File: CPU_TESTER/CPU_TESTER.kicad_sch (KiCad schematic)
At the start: 27 parts, among them J1 Conn_02x21_Odd_Even, J2 Conn_02x21_Odd_Even, J3 Conn_02x21_Odd_Even, J4 Conn_02x21_Odd_Even, J5 Conn_02x21_Odd_Even, J6 Conn_02x21_Odd_Even, J7 Conn_02x21_Odd_Even, Q1 2N3904, Q2 2N3904, Q3 2N3904

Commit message: CPU tester design
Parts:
- R2, R3, R4, R5, R6, R7: value 10.1K -> 10.5K
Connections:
- net 12V_MON: now also A1.26 (A7); no longer A1.19 (A0)
- net BD_EN0: now also A1.24 (A5); no longer A1.5 (D2)
- net BD_EN1: now also A1.23 (A4); no longer A1.6 (D3)
- net BD_EN2: now also A1.22 (A3); no longer A1.7 (D4)
- net BD_EN3: now also A1.21 (A2); no longer A1.8 (D5)
- net BD_EN4: now also A1.20 (A1); no longer A1.9 (D6)
- net BD_EN5: now also A1.19 (A0); no longer A1.10 (D7)
- net BD_ENM: now also A1.15 (D12); no longer A1.11 (D8)
- net IRQ_0: now also A1.10 (D7); no longer A1.12 (D9)
- net IRQ_1: now also A1.11 (D8); no longer A1.13 (D10)
- net LED_0: now also A1.6 (D3); no longer A1.20 (A1)
- net LED_1: now also A1.8 (D5); no longer A1.21 (A2)
- net LED_2: now also A1.9 (D6); no longer A1.22 (A3)
- net LED_3: now also A1.12 (D9); no longer A1.23 (A4)
- net LED_4: now also A1.13 (D10); no longer A1.24 (A5)
- net LED_5: now also A1.14 (D11); no longer A1.25 (A6)
- net LED_C: now also A1.5 (D2); no longer A1.26 (A7)
- net RST: now also A1.7 (D4); no longer A1.14 (D11)
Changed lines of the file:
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@@
   (no_connect (at 86.36 112.395))
   (no_connect (at 91.44 112.395))
-  (no_connect (at 76.2 153.035))
+  (no_connect (at 101.6 153.035))
   (no_connect (at 76.2 122.555))
   (no_connect (at 76.2 125.095))
@@
     (stroke (width 0) (type default) (color 0 0 0 0))
   )
-  (wire (pts (xy 101.6 153.035) (xy 109.855 153.035))
+  (wire (pts (xy 67.31 153.035) (xy 76.2 153.035))
     (stroke (width 0) (type default) (color 0 0 0 0))
   )
@@
     (effects (font (size 1.27 1.27)) (justify right bottom))
   )
-  (label "BD_EN1" (at 67.31 130.175 0)
-    (effects (font (size 1.27 1.27)) (justify left bottom))
+  (label "BD_EN1" (at 109.855 147.955 180)
+    (effects (font (size 1.27 1.27)) (justify right bottom))
   )
   (label "12V_MON" (at 61.595 93.345 180)
     (effects (font (size 1.27 1.27)) (justify right bottom))
   )
-  (label "IRQ_1" (at 67.31 147.955 0)
+  (label "IRQ_1" (at 67.31 142.875 0)
     (effects (font (size 1.27 1.27)) (justify left bottom))
   )
-  (label "12V_MON" (at 109.855 137.795 180)
+  (label "12V_MON" (at 109.855 155.575 180)
     (effects (font (size 1.27 1.27)) (justify right bottom))
   )
@@
     (effects (font (size 1.27 1.27)) (justify right bottom))
   )
-  (label "BD_EN3" (at 67.31 135.255 0)
-    (effects (font (size 1.27 1.27)) (justify left bottom))
+  (label "BD_EN3" (at 109.855 142.875 180)
+    (effects (font (size 1.27 1.27)) (justify right bottom))
   )
-  (label "BD_ENM" (at 67.31 142.875 0)
+  (label "BD_ENM" (at 67.31 153.035 0)
     (effects (font (size 1.27 1.27)) (justify left bottom))
   )
@@
     (effects (font (size 1.27 1.27)) (justify right bottom))
   )
-  (label "BD_EN5" (at 67.31 140.335 0)
-    (effects (font (size 1.27 1.27)) (justify left bottom))
-  )
-  (label "LED_C" (at 109.855 155.575 180)
+  (label "BD_EN5" (at 109.855 137.795 180)
     (effects (font (size 1.27 1.27)) (justify right bottom))
   )
+  (label "LED_C" (at 67.31 127.635 0)
+    (effects (font (size 1.27 1.27)) (justify left bottom))
+  )
   (label "IRQ_1" (at 127.635 135.89 0)
     (effects (font (size 1.27 1.27)) (justify left bottom))
   )
-  (label "LED_1" (at 109.855 142.875 180)
-    (effects (font (size 1.27 1.27)) (justify right bottom))
+  (label "LED_1" (at 67.31 135.255 0)
+    (effects (font (size 1.27 1.27)) (justify left bottom))
   )
   (label "IRQ_0" (at 110.49 110.49 0)
     (effects (font (size 1.27 1.27)) (justify left bottom))
   )
-  (label "LED_3" (at 109.855 147.955 180)
-    (effects (font (size 1.27 1.27)) (justify right bottom))
+  (label "LED_3" (at 67.31 145.415 0)
+    (effects (font (size 1.27 1.27)) (justify left bottom))
   )
-  (label "RST" (at 67.31 150.495 0)
+  (label "RST" (at 67.31 132.715 0)
     (effects (font (size 1.27 1.27)) (justify left bottom))
   )
@@
     (effects (font (size 1.27 1.27)) (justify right bottom))
   )
-  (label "LED_4" (at 109.855 150.495 180)
-    (effects (font (size 1.27 1.27)) (justify right bottom))
-  )
-  (label "IRQ_0" (at 67.31 145.415 0)
+  (label "LED_4" (at 67.31 147.955 0)
     (effects (font (size 1.27 1.27)) (justify left bottom))
   )
-  (label "BD_EN2" (at 67.31 132.715 0)
+  (label "IRQ_0" (at 67.31 140.335 0)
     (effects (font (size 1.27 1.27)) (justify left bottom))
   )
-  (label "LED_0" (at 109.855 140.335 180)
+  (label "BD_EN2" (at 109.855 145.415 180)
     (effects (font (size 1.27 1.27)) (justify right bottom))
   )
+  (label "LED_0" (at 67.31 130.175 0)
+    (effects (font (size 1.27 1.27)) (justify left bottom))
+  )
   (label "LED_3" (at 44.45 150.495 180)
     (effects (font (size 1.27 1.27)) (justify right bottom))
   )
-  (label "BD_EN0" (at 67.31 127.635 0)
-    (effects (font (size 1.27 1.27)) (justify left bottom))
-  )
-  (label "BD_EN4" (at 67.31 137.795 0)
-    (effects (font (size 1.27 1.27)) (justify left bottom))
+  (label "BD_EN0" (at 109.855 150.495 180)
+    (effects (font (size 1.27 1.27)) (justify right bottom))
   )
-  (label "LED_2" (at 109.855 145.415 180)
+  (label "BD_EN4" (at 109.855 140.335 180)
     (effects (font (size 1.27 1.27)) (justify right bottom))
   )
+  (label "LED_2" (at 67.31 137.795 0)
+    (effects (font (size 1.27 1.27)) (justify left bottom))
+  )
   (label "LED_0" (at 44.45 110.49 180)
     (effects (font (size 1.27 1.27)) (justify right bottom))
   )
-  (label "LED_5" (at 109.855 153.035 180)
-    (effects (font (size 1.27 1.27)) (justify right bottom))
+  (label "LED_5" (at 67.31 150.495 0)
+    (effects (font (size 1.27 1.27)) (justify left bottom))
   )
   (label "LED_2" (at 44.45 137.16 180)
@@
     (in_bom yes) (on_board yes) (fields_autoplaced)
     (property "Reference" "R2" (id 0) (at 121.285 104.14 90))
-    (property "Value" "10.1K" (id 1) (at 121.285 106.68 90))
+    (property "Value" "10.5K" (id 1) (at 121.285 106.68 90))
     (property "Footprint" "Resistor_THT:R_Axial_DIN0207_L6.3mm_D2.5mm_P10.16mm_Horizontal" (id 2) (at 121.285 112.268 90)
       (effects (font (size 1.27 1.27)) hide)
@@
       (effects (font (size 1.27 1.27)) (justify left))
     )
-    (property "Value" "10.1K" (id 1) (at 154.305 165.7349 0)
+    (property "Value" "10.5K" (id 1) (at 154.305 165.7349 0)
       (effects (font (size 1.27 1.27)) (justify left))
     )
@@
       (effects (font (size 1.27 1.27)) (justify left))
     )
-    (property "Value" "10.1K" (id 1) (at 154.305 125.7299 0)
+    (property "Value" "10.5K" (id 1) (at 154.305 125.7299 0)
       (effects (font (size 1.27 1.27)) (justify left))
     )
@@
     (in_bom yes) (on_board yes) (fields_autoplaced)
     (property "Reference" "R5" (id 0) (at 139.065 169.545 90))
-    (property "Value" "10.1K" (id 1) (at 139.065 172.085 90))
+    (property "Value" "10.5K" (id 1) (at 139.065 172.085 90))
     (property "Footprint" "Resistor_THT:R_Axial_DIN0207_L6.3mm_D2.5mm_P10.16mm_Horizontal" (id 2) (at 139.065 177.673 90)
       (effects (font (size 1.27 1.27)) hide)
@@
       (effects (font (size 1.27 1.27)) (justify left))
     )
-    (property "Value" "10.1K" (id 1) (at 136.525 100.3299 0)
+    (property "Value" "10.5K" (id 1) (at 136.525 100.3299 0)
       (effects (font (size 1.27 1.27)) (justify left))
     )
@@
     (in_bom yes) (on_board yes) (fields_autoplaced)
     (property "Reference" "R4" (id 0) (at 139.065 129.54 90))
-    (property "Value" "10.1K" (id 1) (at 139.065 132.08 90))
+    (property "Value" "10.5K" (id 1) (at 139.065 132.08 90))
     (property "Footprint" "Resistor_THT:R_Axial_DIN0207_L6.3mm_D2.5mm_P10.16mm_Horizontal" (id 2) (at 139.065 137.668 90)
       (effects (font (size 1.27 1.27)) hide)
@@
     )
     (path "/146bb74a-c5dc-4101-86b1-cd35181b91ef"
-      (reference "R2") (unit 1) (value "10.1K") (footprint "Resistor_THT:R_Axial_DIN0207_L6.3mm_D2.5mm_P10.16mm_Horizontal")
+      (reference "R2") (unit 1) (value "10.5K") (footprint "Resistor_THT:R_Axial_DIN0207_L6.3mm_D2.5mm_P10.16mm_Horizontal")
     )
     (path "/dd175bfa-b3ad-4339-abd5-bbb7c0154b85"
-      (reference "R3") (unit 1) (value "10.1K") (footprint "Resistor_THT:R_Axial_DIN0207_L6.3mm_D2.5mm_P10.16mm_Horizontal")
+      (reference "R3") (unit 1) (value "10.5K") (footprint "Resistor_THT:R_Axial_DIN0207_L6.3mm_D2.5mm_P10.16mm_Horizontal")
     )
     (path "/ede24277-117d-4b1a-99a2-30baade9bd49"
-      (reference "R4") (unit 1) (value "10.1K") (footprint "Resistor_THT:R_Axial_DIN0207_L6.3mm_D2.5mm_P10.16mm_Horizontal")
+      (reference "R4") (unit 1) (value "10.5K") (footprint "Resistor_THT:R_Axial_DIN0207_L6.3mm_D2.5mm_P10.16mm_Horizontal")
     )
     (path "/c0a6a793-23e6-4787-a4b7-0b60fe74897d"
-      (reference "R5") (unit 1) (value "10.1K") (footprint "Resistor_THT:R_Axial_DIN0207_L6.3mm_D2.5mm_P10.16mm_Horizontal")
+      (reference "R5") (unit 1) (value "10.5K") (footprint "Resistor_THT:R_Axial_DIN0207_L6.3mm_D2.5mm_P10.16mm_Horizontal")
     )
     (path "/ac35a4cd-ee98-4a72-92c9-79826d438297"
-      (reference "R6") (unit 1) (value "10.1K") (footprint "Resistor_THT:R_Axial_DIN0207_L6.3mm_D2.5mm_P10.16mm_Horizontal")
+      (reference "R6") (unit 1) (value "10.5K") (footprint "Resistor_THT:R_Axial_DIN0207_L6.3mm_D2.5mm_P10.16mm_Horizontal")
     )
     (path "/9bdb9f7f-025a-4cbb-add4-7af250ed0474"
-      (reference "R7") (unit 1) (value "10.1K") (footprint "Resistor_THT:R_Axial_DIN0207_L6.3mm_D2.5mm_P10.16mm_Horizontal")
+      (reference "R7") (unit 1) (value "10.5K") (footprint "Resistor_THT:R_Axial_DIN0207_L6.3mm_D2.5mm_P10.16mm_Horizontal")
     )
     (path "/27ba8598-88b0-4157-a7a7-e1e74e09d01a"

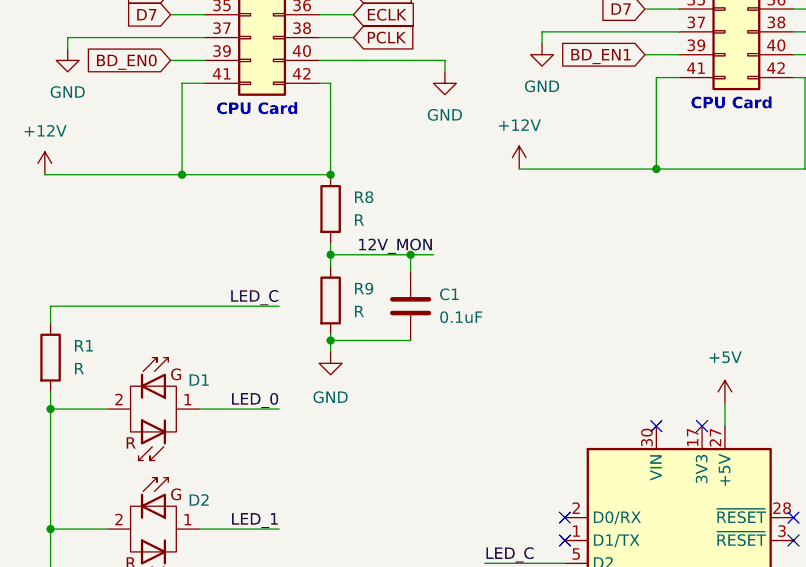
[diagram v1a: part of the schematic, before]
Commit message: Updated tester schematic, per built
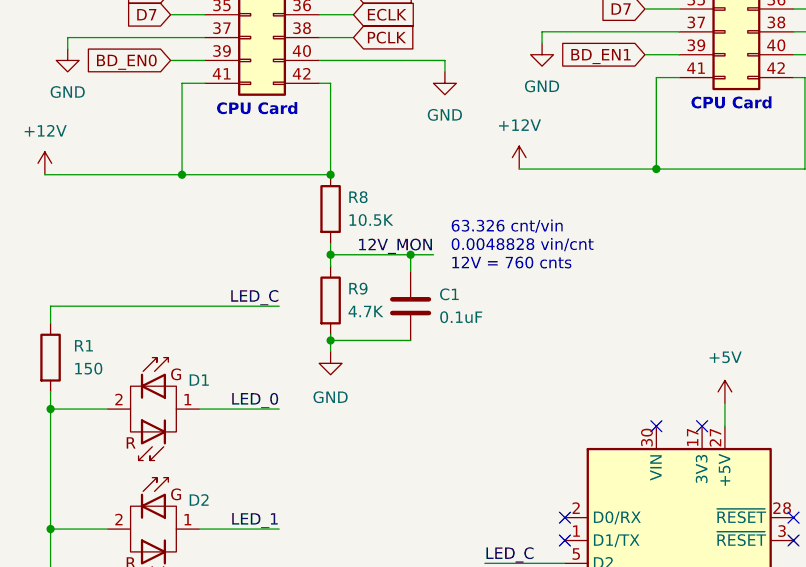
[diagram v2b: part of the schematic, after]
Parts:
- R1: value R -> 150
- R8: value R -> 10.5K
- R9: value R -> 4.7K
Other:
- note added: "63.326 cnt/vin 0.0048828 vin/cnt 12V = 760 cnts"
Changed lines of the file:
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@@
     (effects (font (size 1.27 1.27) (thickness 0.254) bold) (justify left bottom))
   )
+  (text "63.326 cnt/vin\n0.0048828 vin/cnt\n12V = 760 cnts" (at 63.5 95.25 0)
+    (effects (font (size 1.27 1.27)) (justify left bottom))
+  )
   (text "CPU Card" (at 140.335 76.835 0)
     (effects (font (size 1.27 1.27) (thickness 0.254) bold) (justify left bottom))
@@
       (effects (font (size 1.27 1.27)) (justify left))
     )
-    (property "Value" "R" (id 1) (at 21.59 106.0449 0)
+    (property "Value" "150" (id 1) (at 21.59 106.0449 0)
       (effects (font (size 1.27 1.27)) (justify left))
     )
@@
   (symbol (lib_id "Device:R") (at 50.165 88.265 0) (unit 1)
     (in_bom yes) (on_board yes) (fields_autoplaced)
-    (property "Reference" "R8" (id 0) (at 52.705 86.9949 0)
+    (property "Reference" "R8" (id 0) (at 52.07 86.9949 0)
       (effects (font (size 1.27 1.27)) (justify left))
     )
-    (property "Value" "R" (id 1) (at 52.705 89.5349 0)
+    (property "Value" "10.5K" (id 1) (at 52.07 89.5349 0)
       (effects (font (size 1.27 1.27)) (justify left))
     )
@@
   (symbol (lib_id "Device:R") (at 50.165 98.425 0) (unit 1)
     (in_bom yes) (on_board yes) (fields_autoplaced)
-    (property "Reference" "R9" (id 0) (at 52.705 97.1549 0)
+    (property "Reference" "R9" (id 0) (at 52.07 97.1549 0)
       (effects (font (size 1.27 1.27)) (justify left))
     )
-    (property "Value" "R" (id 1) (at 52.705 99.6949 0)
+    (property "Value" "4.7K" (id 1) (at 52.07 99.6949 0)
       (effects (font (size 1.27 1.27)) (justify left))
     )
@@
     )
     (path "/16bab16a-81e3-4cea-b722-6923ddb77221"
-      (reference "R1") (unit 1) (value "R") (footprint "Resistor_THT:R_Axial_DIN0207_L6.3mm_D2.5mm_P10.16mm_Horizontal")
+      (reference "R1") (unit 1) (value "150") (footprint "Resistor_THT:R_Axial_DIN0207_L6.3mm_D2.5mm_P10.16mm_Horizontal")
     )
     (path "/146bb74a-c5dc-4101-86b1-cd35181b91ef"
@@
     )
     (path "/27ba8598-88b0-4157-a7a7-e1e74e09d01a"
-      (reference "R8") (unit 1) (value "R") (footprint "Resistor_THT:R_Axial_DIN0207_L6.3mm_D2.5mm_P10.16mm_Horizontal")
+      (reference "R8") (unit 1) (value "10.5K") (footprint "Resistor_THT:R_Axial_DIN0207_L6.3mm_D2.5mm_P10.16mm_Horizontal")
     )
     (path "/4acba49d-9814-405c-a4ec-97a0e5647424"
-      (reference "R9") (unit 1) (value "R") (footprint "Resistor_THT:R_Axial_DIN0207_L6.3mm_D2.5mm_P10.16mm_Horizontal")
+      (reference "R9") (unit 1) (value "4.7K") (footprint "Resistor_THT:R_Axial_DIN0207_L6.3mm_D2.5mm_P10.16mm_Horizontal")
     )
   )

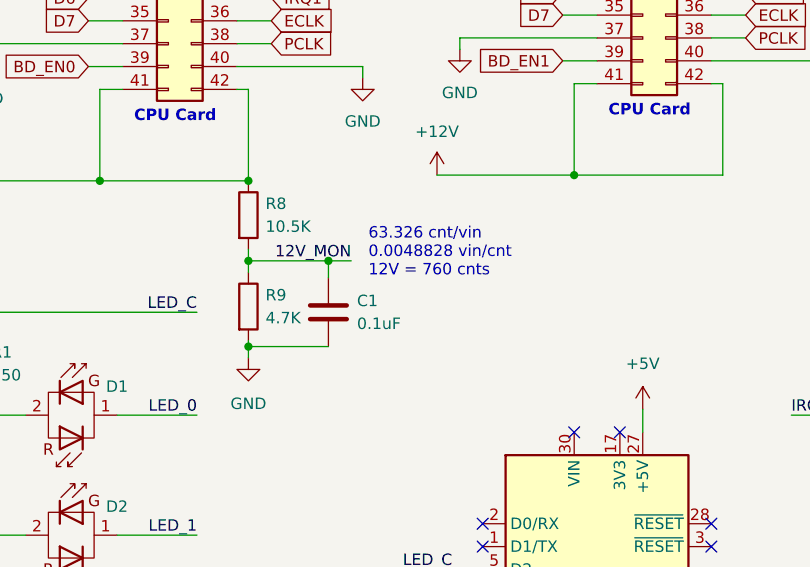
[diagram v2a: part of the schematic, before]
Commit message: Updated voltage monitoring divider to as-built.
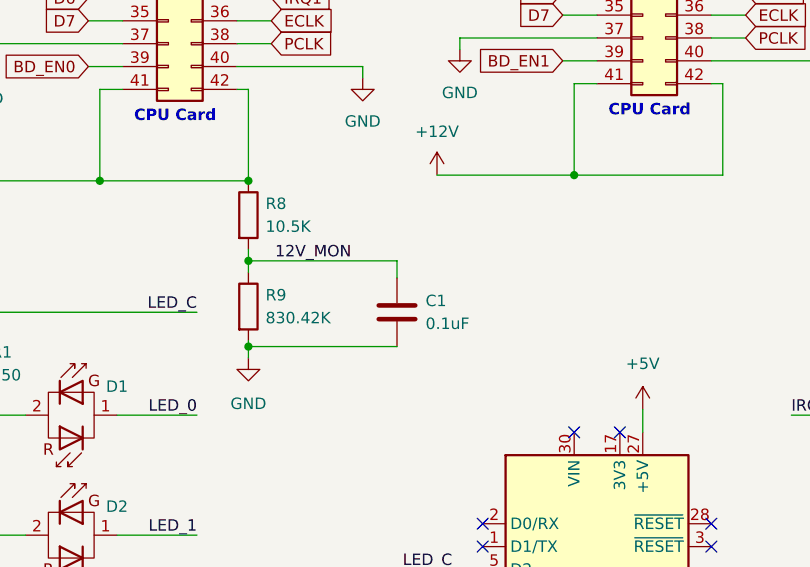
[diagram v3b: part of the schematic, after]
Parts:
- R9: value 4.7K -> 830.42K
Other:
- note removed: "63.326 cnt/vin 0.0048828 vin/cnt 12V = 760 cnts"
- moved on the sheet: C1
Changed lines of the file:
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@@
   (junction (at 187.96 83.185) (diameter 0) (color 0 0 0 0)
   )
-  (junction (at 59.055 93.345) (diameter 0) (color 0 0 0 0)
-  )
   (junction (at 19.05 163.83) (diameter 0) (color 0 0 0 0)
   )
@@
     (stroke (width 0) (type default) (color 0 0 0 0))
   )
-  (wire (pts (xy 59.055 93.345) (xy 61.595 93.345))
-    (stroke (width 0) (type default) (color 0 0 0 0))
-  )
   (wire (pts (xy 32.385 53.975) (xy 36.195 53.975))
     (stroke (width 0) (type default) (color 0 0 0 0))
@@
     (stroke (width 0) (type default) (color 0 0 0 0))
   )
-  (wire (pts (xy 50.165 93.345) (xy 59.055 93.345))
+  (wire (pts (xy 50.165 93.345) (xy 66.675 93.345))
     (stroke (width 0) (type default) (color 0 0 0 0))
   )
@@
     (stroke (width 0) (type default) (color 0 0 0 0))
   )
-  (wire (pts (xy 50.165 102.87) (xy 59.055 102.87))
+  (wire (pts (xy 50.165 102.87) (xy 66.675 102.87))
     (stroke (width 0) (type default) (color 0 0 0 0))
   )
@@
     (stroke (width 0) (type default) (color 0 0 0 0))
   )
-  (wire (pts (xy 59.055 93.345) (xy 59.055 95.25))
-    (stroke (width 0) (type default) (color 0 0 0 0))
-  )
   (wire (pts (xy 175.26 67.945) (xy 175.26 69.215))
     (stroke (width 0) (type default) (color 0 0 0 0))
@@
     (stroke (width 0) (type default) (color 0 0 0 0))
   )
+  (wire (pts (xy 66.675 95.25) (xy 66.675 93.345))
+    (stroke (width 0) (type default) (color 0 0 0 0))
+  )
   (wire (pts (xy 151.765 180.975) (xy 151.765 182.245))
     (stroke (width 0) (type default) (color 0 0 0 0))
@@
     (effects (font (size 1.27 1.27) (thickness 0.254) bold) (justify left bottom))
   )
-  (text "63.326 cnt/vin\n0.0048828 vin/cnt\n12V = 760 cnts" (at 63.5 95.25 0)
-    (effects (font (size 1.27 1.27)) (justify left bottom))
-  )
   (text "CPU Card" (at 140.335 76.835 0)
     (effects (font (size 1.27 1.27) (thickness 0.254) bold) (justify left bottom))
@@
       (effects (font (size 1.27 1.27)) (justify left))
     )
-    (property "Value" "4.7K" (id 1) (at 52.07 99.6949 0)
+    (property "Value" "830.42K" (id 1) (at 52.07 99.6949 0)
       (effects (font (size 1.27 1.27)) (justify left))
     )
@@
     (pin "1")
   )
-  (symbol (lib_id "Device:C") (at 59.055 99.06 0) (unit 1)
+  (symbol (lib_id "Device:C") (at 66.675 99.06 0) (unit 1)
     (in_bom yes) (on_board yes) (fields_autoplaced)
-    (property "Reference" "C1" (id 0) (at 62.23 97.7899 0)
+    (property "Reference" "C1" (id 0) (at 69.85 97.7899 0)
       (effects (font (size 1.27 1.27)) (justify left))
     )
-    (property "Value" "0.1uF" (id 1) (at 62.23 100.3299 0)
+    (property "Value" "0.1uF" (id 1) (at 69.85 100.3299 0)
       (effects (font (size 1.27 1.27)) (justify left))
     )
-    (property "Footprint" "Capacitor_THT:C_Rect_L7.2mm_W3.0mm_P5.00mm_FKS2_FKP2_MKS2_MKP2" (id 2) (at 60.0202 102.87 0)
+    (property "Footprint" "Capacitor_THT:C_Rect_L7.2mm_W3.0mm_P5.00mm_FKS2_FKP2_MKS2_MKP2" (id 2) (at 67.6402 102.87 0)
       (effects (font (size 1.27 1.27)) hide)
     )
-    (property "Datasheet" "~" (id 3) (at 59.055 99.06 0)
+    (property "Datasheet" "~" (id 3) (at 66.675 99.06 0)
       (effects (font (size 1.27 1.27)) hide)
     )
@@
     )
     (path "/4acba49d-9814-405c-a4ec-97a0e5647424"
-      (reference "R9") (unit 1) (value "4.7K") (footprint "Resistor_THT:R_Axial_DIN0207_L6.3mm_D2.5mm_P10.16mm_Horizontal")
+      (reference "R9") (unit 1) (value "830.42K") (footprint "Resistor_THT:R_Axial_DIN0207_L6.3mm_D2.5mm_P10.16mm_Horizontal")
     )
   )
